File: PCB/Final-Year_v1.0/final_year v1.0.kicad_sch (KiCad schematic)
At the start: 34 parts, among them J1 Power In, J2 Screw_Terminal_01x07, J3 Screw_Terminal_01x03, J4 Screw_Terminal_01x04, J5 Screw_Terminal_01x03, J6 PT1000, J7 HCPV 22x, J8 LDR_module, U1 LM7805_TO220, U2 TL431LP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

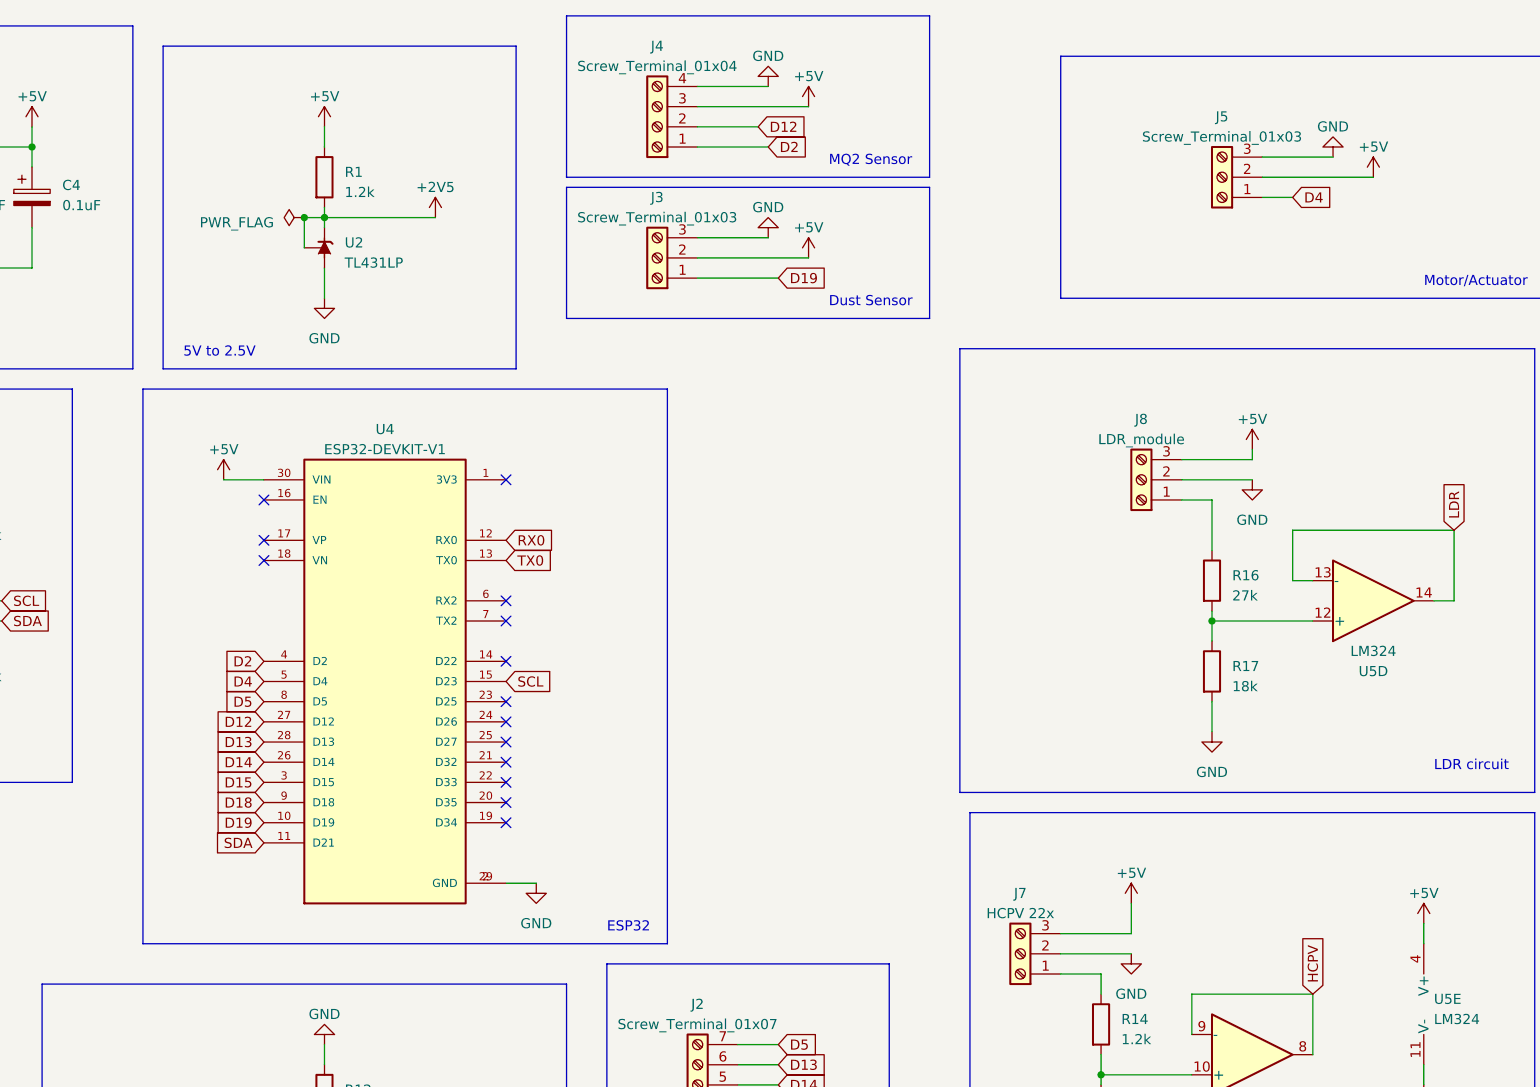
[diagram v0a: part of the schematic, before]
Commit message: no crc errors now
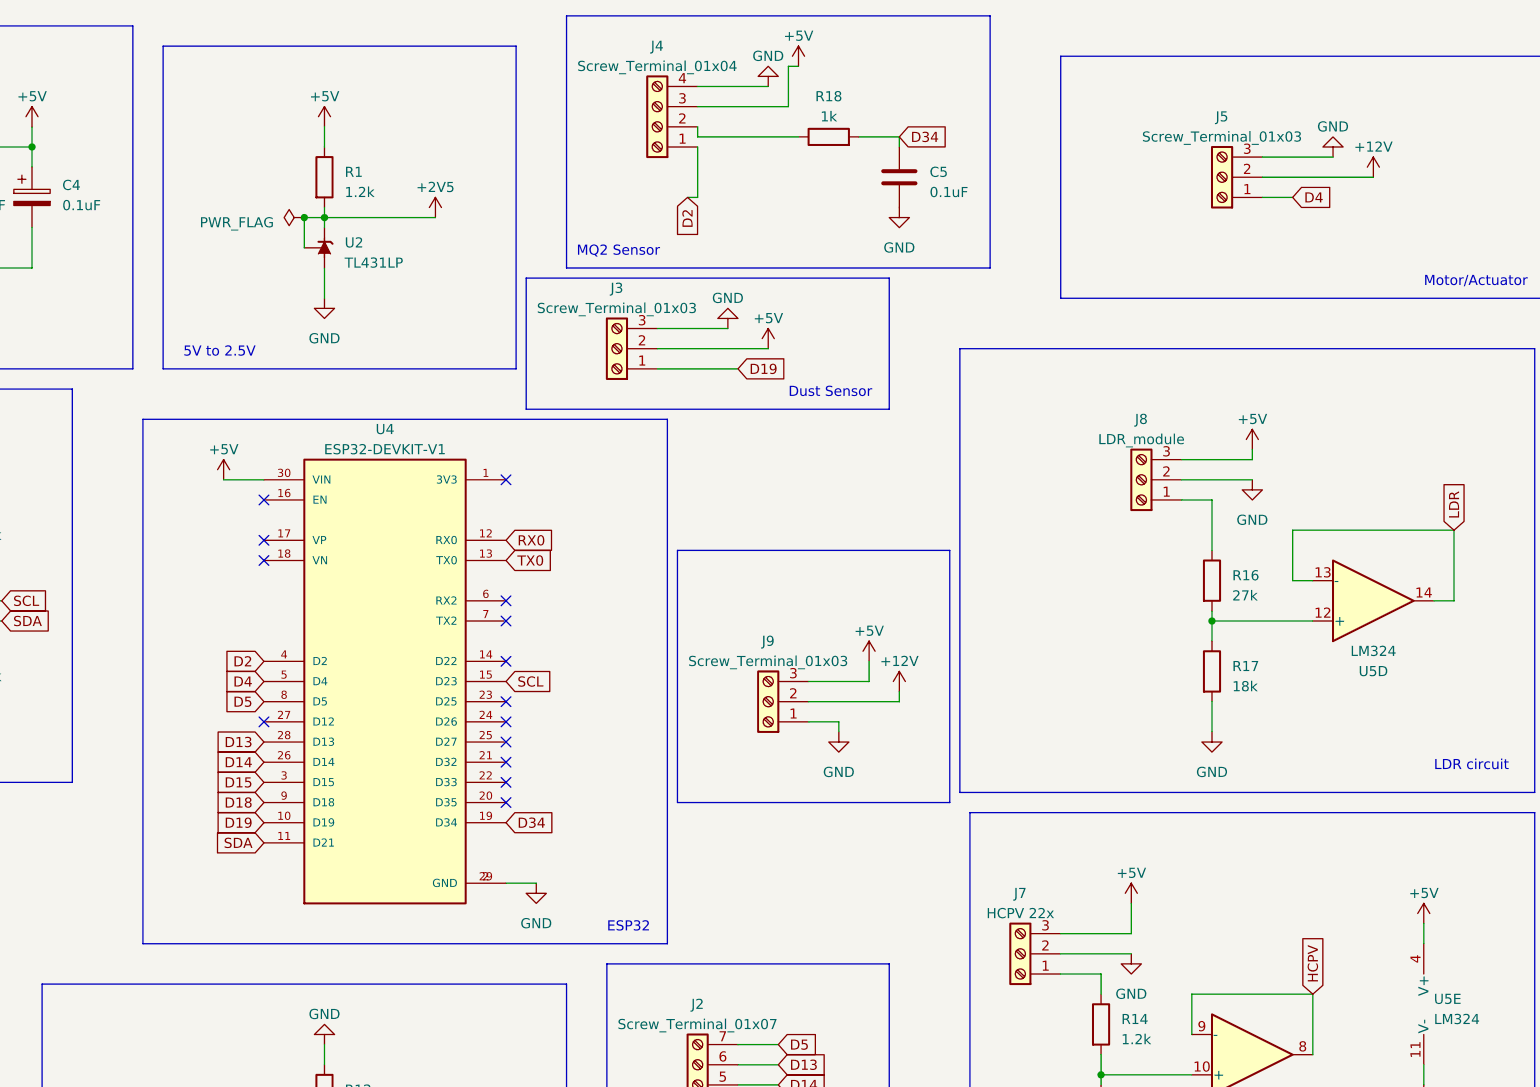
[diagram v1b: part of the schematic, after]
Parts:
- added C5: 0.1uF, symbol Device:C
- added J9: Screw_Terminal_01x03, symbol Connector:Screw_Terminal_01x03
- added R18: 1k, symbol Device:R
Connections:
- net +12V: now also J5.2 (Pin_2), J9.2 (Pin_2)
- net +5V: now also J9.3 (Pin_3); no longer J5.2 (Pin_2)
- net GND: now also C5.2, J9.1 (Pin_1)
- net D34: now reaches U4.19 (D34)
- net D34: now also C5.1, R18.2
- net D12: no longer names the net of J4.2 (Pin_2)
- net D12: now also R18.1; no longer U4.27 (D12)
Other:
- moved on the sheet: J3

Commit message: Add files via upload
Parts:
- removed J8: LDR_module, symbol Connector:Screw_Terminal_01x03
- added J8: Conn_01x03_Pin, Connector_PinHeader_2.54mm:PinHeader_1x03_P2.54mm_Vertical, symbol Connector:Conn_01x03_Pin
- C1, C4, C5: footprint (none) -> Capacitor_THT:C_Disc_D6.0mm_W2.5mm_P5.00mm
- C2: footprint (none) -> Capacitor_THT:C_Radial_D6.3mm_H7.0mm_P2.50mm
- C3: footprint (none) -> Capacitor_THT:C_Radial_D6.3mm_H5.0mm_P2.50mm
- J1, J6: footprint (none) -> TerminalBlock_Phoenix:TerminalBlock_Phoenix_MKDS-1,5-2-5.08_1x02_P5.08mm_Horizontal
- J2: footprint (none) -> TerminalBlock_Phoenix:TerminalBlock_Phoenix_MKDS-1,5-7-5.08_1x07_P5.08mm_Horizontal
- J3, J5, J7, J9: footprint (none) -> TerminalBlock_Phoenix:TerminalBlock_Phoenix_MKDS-1,5-3-5.08_1x03_P5.08mm_Horizontal
- J4: footprint (none) -> TerminalBlock_Phoenix:TerminalBlock_Phoenix_MKDS-1,5-4-5.08_1x04_P5.08mm_Horizontal
- R1, R10, R11, R12, R13, R14, R15, R16, R17, R18, R2, R3, R4, R5, R6, R7, R8, R9: footprint (none) -> Resistor_THT:R_Axial_DIN0207_L6.3mm_D2.5mm_P10.16mm_Horizontal
- U5: footprint (none) -> Package_DIP:DIP-14_W7.62mm
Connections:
- net +5V: now also J8.1 (Pin_1)
- net GND: now also J8.2 (Pin_2)
- net at R16.1: now also J8.3 (Pin_3)
- net D32: now reaches U4.21 (D32)
- net D32: now also J3.1 (Pin_1)
- net D19: no longer names the net of U4.10 (D19)
- net D19: no longer J3.1 (Pin_1)

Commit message: Add files via upload
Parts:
- removed C1, C4: 0.1uF, Capacitor_THT:C_Disc_D6.0mm_W2.5mm_P5.00mm, symbol Device:C_Polarized
- removed J8: Conn_01x03_Pin, Connector_PinHeader_2.54mm:PinHeader_1x03_P2.54mm_Vertical, symbol Connector:Conn_01x03_Pin
- added C4, C6: 0.1uF, Capacitor_THT:C_Disc_D6.0mm_W2.5mm_P5.00mm, symbol Device:C
- added J8: LDR, TerminalBlock_Phoenix:TerminalBlock_Phoenix_MKDS-1,5-3-5.08_1x03_P5.08mm_Horizontal, symbol Connector:Screw_Terminal_01x03
- R13, R9: footprint Resistor_THT:R_Axial_DIN0207_L6.3mm_D2.5mm_P10.16mm_Horizontal -> Resistor_THT:R_Axial_DIN0207_L6.3mm_D2.5mm_P2.54mm_Vertical
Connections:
- net +12V: now also C6.1
- net +5V: now also C4.1, J8.3 (Pin_3)
- net Battery_level: now also U5.7; no longer U5.1
- net GND: now also J6.2 (Pin_2), C4.2, C6.2, J8.2 (Pin_2); no longer J6.1 (Pin_1)
- net PT1000: now also U5.1; no longer U5.7
- net at R7.2, R8.1: now also U5.5 (+); no longer U5.3 (+)
- net at R11.2, R12.2, R13.1: now also U5.2 (-); no longer U5.6 (-)
- net at R4.2, R6.2, R9.1: now also U5.6 (-); no longer U5.2 (-)
- net at R16.1: now also J8.1 (Pin_1)
- new net: J6.1 (Pin_1), R10.2, U5.3 (+)
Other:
- moved on the sheet: J6, U5A, U5B

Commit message: Add files via upload
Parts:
- added BZ1: Buzzer, Buzzer_Beeper:Buzzer_15x7.5RM7.6, symbol Device:Buzzer
- added C1: 0.1u, Capacitor_THT:C_Disc_D6.0mm_W2.5mm_P5.00mm, symbol Device:C
- added C7: 10nF, Capacitor_THT:C_Disc_D3.8mm_W2.6mm_P2.50mm, symbol Device:C
- added C8: 0.1uF, Capacitor_THT:C_Disc_D6.0mm_W2.5mm_P5.00mm, symbol Device:C
- added D1: LED, LED_THT:LED_D5.0mm, symbol Device:LED
- added Q1: BC547, Package_TO_SOT_THT:TO-92_Inline, symbol Transistor_BJT:BC547
- added R19: 1.2k, Resistor_THT:R_Axial_DIN0207_L6.3mm_D2.5mm_P10.16mm_Horizontal, symbol Device:R
- added R20: 330, Resistor_THT:R_Axial_DIN0207_L6.3mm_D2.5mm_P10.16mm_Horizontal, symbol Device:R
- C2: footprint Capacitor_THT:C_Radial_D6.3mm_H7.0mm_P2.50mm -> Capacitor_THT:CP_Radial_D4.0mm_P2.00mm
- C3: footprint Capacitor_THT:C_Radial_D6.3mm_H5.0mm_P2.50mm -> Capacitor_THT:CP_Radial_D4.0mm_P2.00mm
- J5: value Screw_Terminal_01x03 -> Actuator
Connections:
- net +12V: now also BZ1.1 (-)
- net Battery_level: now also U6.1 (A3); no longer U6.2 (A2)
- net D13: now also J2.1 (Pin_1); no longer J2.6 (Pin_6)
- net D14: now also J2.2 (Pin_2); no longer J2.5 (Pin_5)
- net D15: now also J2.6 (Pin_6); no longer J2.4 (Pin_4)
- net D18: now also J2.5 (Pin_5); no longer J2.3 (Pin_3)
- net GND: now also U6.6 (ADDR), C1.2, C7.2, C8.1, D1.1 (K), Q1.3 (E)
- net HCPV: now also U6.4 (A0); no longer U6.3 (A1)
- net LDR: now also U6.3 (A1); no longer U6.1 (A3)
- net PT1000: now also U6.2 (A2); no longer U6.4 (A0)
- net RX0: now also J2.4 (Pin_4); no longer J2.2 (Pin_2)
- net TX0: now also J2.3 (Pin_3); no longer J2.1 (Pin_1)
- net at J6.1 (Pin_1), R10.2, U5.3 (+): now also C8.2
- net at R7.2, R8.1, U5.5 (+): now also C7.1
- net D33: now reaches U4.22 (D33)
- net D33: now also R19.2
- net D12: now reaches U4.27 (D12)
- net D12: now also R20.1
- net at R16.2, R17.1, U5.12 (+): now also C1.1
- new net: BZ1.2 (+), Q1.1 (C)
- new net: Q1.2 (B), R19.1
- new net: D1.2 (A), R20.2
- no-connect marks 16 -> 13
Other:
- note added: "Buzzer"
- note added: "LED"

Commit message: Add files via upload
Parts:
- added H1, H2, H3, H4: MountingHole, MountingHole:MountingHole_3.2mm_M3, symbol Mechanical:MountingHole
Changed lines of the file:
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@@
+    )
+  )
+  (symbol (lib_id "Mechanical:MountingHole") (at 306.07 109.22 0) (unit 1)
+    (in_bom yes) (on_board yes) (dnp no) (fields_autoplaced)
+    (property "Reference" "H1" (at 308.61 108.585 0)
+      (effects (font (size 1.27 1.27)) (justify left))
+    )
+    (property "Value" "MountingHole" (at 308.61 111.125 0)
+      (effects (font (size 1.27 1.27)) (justify left))
+    )
+    (property "Footprint" "MountingHole:MountingHole_3.2mm_M3" (at 306.07 109.22 0)
+      (effects (font (size 1.27 1.27)) hide)
+    )
+    (property "Datasheet" "~" (at 306.07 109.22 0)
+      (effects (font (size 1.27 1.27)) hide)
+    )
+    (instances
+      (project "final_year v1.0"
+        (path "/49226e52-308e-4c85-869a-6307490999e3"
+          (reference "H1") (unit 1)
+        )
+      )
     )
   )
@@
         (path "/49226e52-308e-4c85-869a-6307490999e3"
           (reference "R2") (unit 1)
+        )
+      )
+    )
+  )
+  (symbol (lib_id "Mechanical:MountingHole") (at 306.07 121.92 0) (unit 1)
+    (in_bom yes) (on_board yes) (dnp no) (fields_autoplaced)
+    (property "Reference" "H3" (at 308.61 121.285 0)
+      (effects (font (size 1.27 1.27)) (justify left))
+    )
+    (property "Value" "MountingHole" (at 308.61 123.825 0)
+      (effects (font (size 1.27 1.27)) (justify left))
+    )
+    (property "Footprint" "MountingHole:MountingHole_3.2mm_M3" (at 306.07 121.92 0)
+      (effects (font (size 1.27 1.27)) hide)
+    )
+    (property "Datasheet" "~" (at 306.07 121.92 0)
+      (effects (font (size 1.27 1.27)) hide)
+    )
+    (instances
+      (project "final_year v1.0"
+        (path "/49226e52-308e-4c85-869a-6307490999e3"
+          (reference "H3") (unit 1)
+        )
+      )
+    )
+  )
+  (symbol (lib_id "Mechanical:MountingHole") (at 306.07 115.57 0) (unit 1)
+    (in_bom yes) (on_board yes) (dnp no) (fields_autoplaced)
+    (property "Reference" "H2" (at 308.61 114.935 0)
+      (effects (font (size 1.27 1.27)) (justify left))
+    )
+    (property "Value" "MountingHole" (at 308.61 117.475 0)
+      (effects (font (size 1.27 1.27)) (justify left))
+    )
+    (property "Footprint" "MountingHole:MountingHole_3.2mm_M3" (at 306.07 115.57 0)
+      (effects (font (size 1.27 1.27)) hide)
+    )
+    (property "Datasheet" "~" (at 306.07 115.57 0)
+      (effects (font (size 1.27 1.27)) hide)
+    )
+    (instances
+      (project "final_year v1.0"
+        (path "/49226e52-308e-4c85-869a-6307490999e3"
+          (reference "H2") (unit 1)
         )
       )
@@
         )
       )
+    )
+  )
+  (symbol (lib_id "Mechanical:MountingHole") (at 306.07 128.27 0) (unit 1)
+    (in_bom yes) (on_board yes) (dnp no) (fields_autoplaced)
+    (property "Reference" "H4" (at 308.61 127.635 0)
+      (effects (font (size 1.27 1.27)) (justify left))
+    )
+    (property "Value" "MountingHole" (at 308.61 130.175 0)
+      (effects (font (size 1.27 1.27)) (justify left))
+    )
+    (property "Footprint" "MountingHole:MountingHole_3.2mm_M3" (at 306.07 128.27 0)
+      (effects (font (size 1.27 1.27)) hide)
+    )
+    (property "Datasheet" "~" (at 306.07 128.27 0)
+      (effects (font (size 1.27 1.27)) hide)
+    )
+    (instances
+      (project "final_year v1.0"
+        (path "/49226e52-308e-4c85-869a-6307490999e3"
+          (reference "H4") (unit 1)
+        )
+      )
